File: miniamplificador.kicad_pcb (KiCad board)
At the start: 2 copper layers, 13 parts, among them CON1 A0 OUT ARDUINO, CON2 D6 IN ARDUINO, J1 Audio-Jack-3, Q1 BC547, SW1 Singnal Select

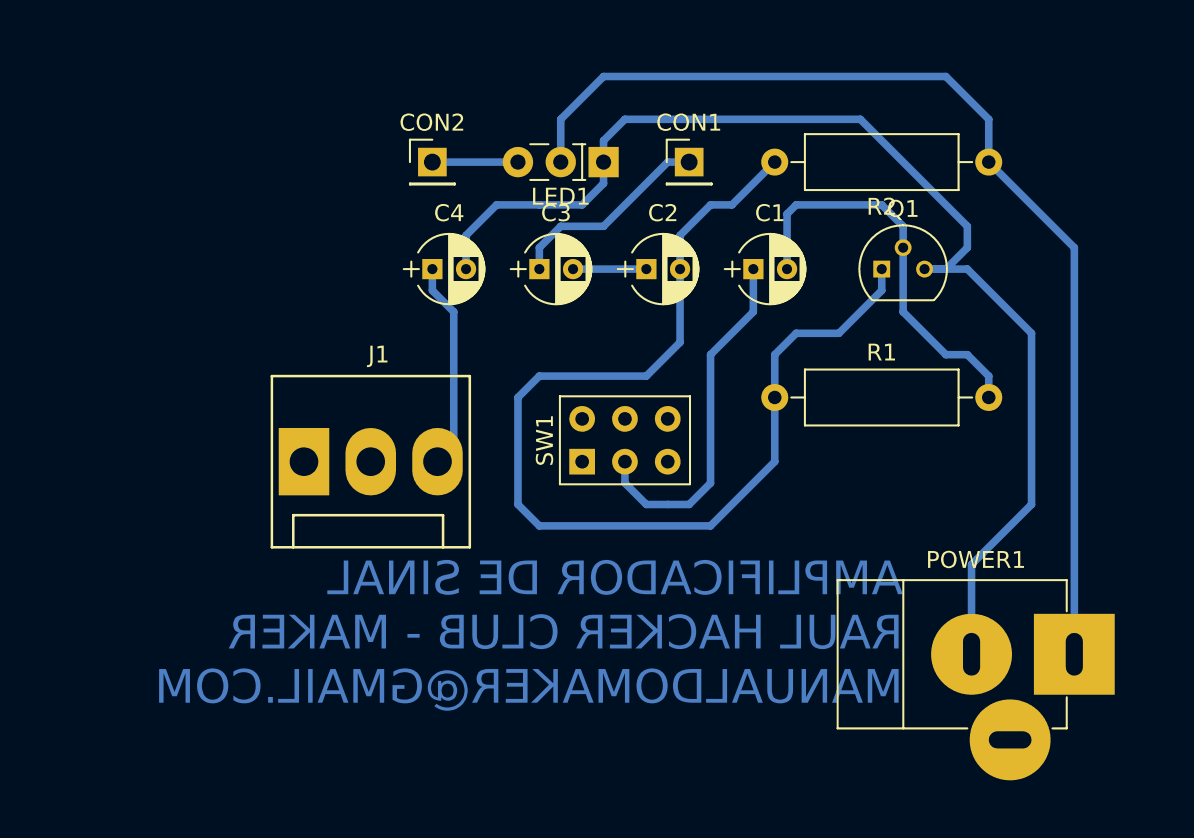
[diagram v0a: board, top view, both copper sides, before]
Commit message: Fechamento das trilhas da placa
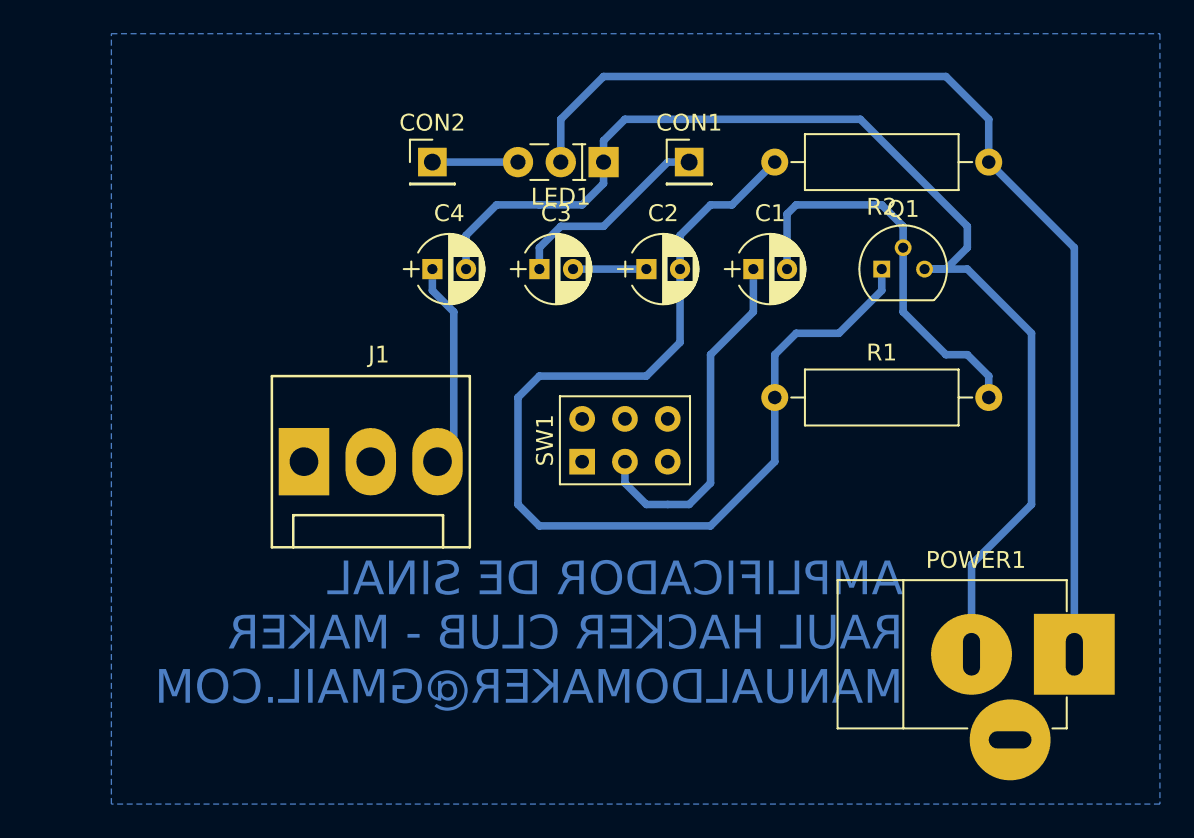
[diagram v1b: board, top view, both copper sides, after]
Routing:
- added copper zone on B.Cu, net (none)
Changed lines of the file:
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@@
     (links 17)
     (no_connects 2)
-    (area 126.30714 82.174999 184.485001 124.795001)
+    (area 124.46 80.01 186.690001 125.730001)
     (thickness 1.6)
     (drawings 1)
@@
   (segment (start 153.67 82.55) (end 151.13 85.09) (width 0.45) (layer B.Cu) (net 11))
   (segment (start 151.13 85.09) (end 151.13 87.63) (width 0.45) (layer B.Cu) (net 11))
+  (zone (net 0) (net_name "") (layer B.Cu) (hatch edge 0.508)
+    (connect_pads (clearance 0.508))
+    (min_thickness 0.254)
+    (fill yes (arc_segments 16) (thermal_gap 0.508) (thermal_bridge_width 0.508))
+    (polygon
+      (pts
+        (xy 186.69 125.73) (xy 124.46 125.73) (xy 124.46 80.01) (xy 186.69 80.01)
+      )
+    )
+  )
 )
